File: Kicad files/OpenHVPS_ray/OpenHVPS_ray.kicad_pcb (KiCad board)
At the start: 2 copper layers, 40.6 x 20.8 mm, 67 parts, among them J2 Conn_01x03_Male, Q1 FQT7N10, Q2 BC846A, Q3 MMDT3906, U1 MAX6008AEUR+T, U2 74HC14, U3 MAX4162, U4 CD14538BM

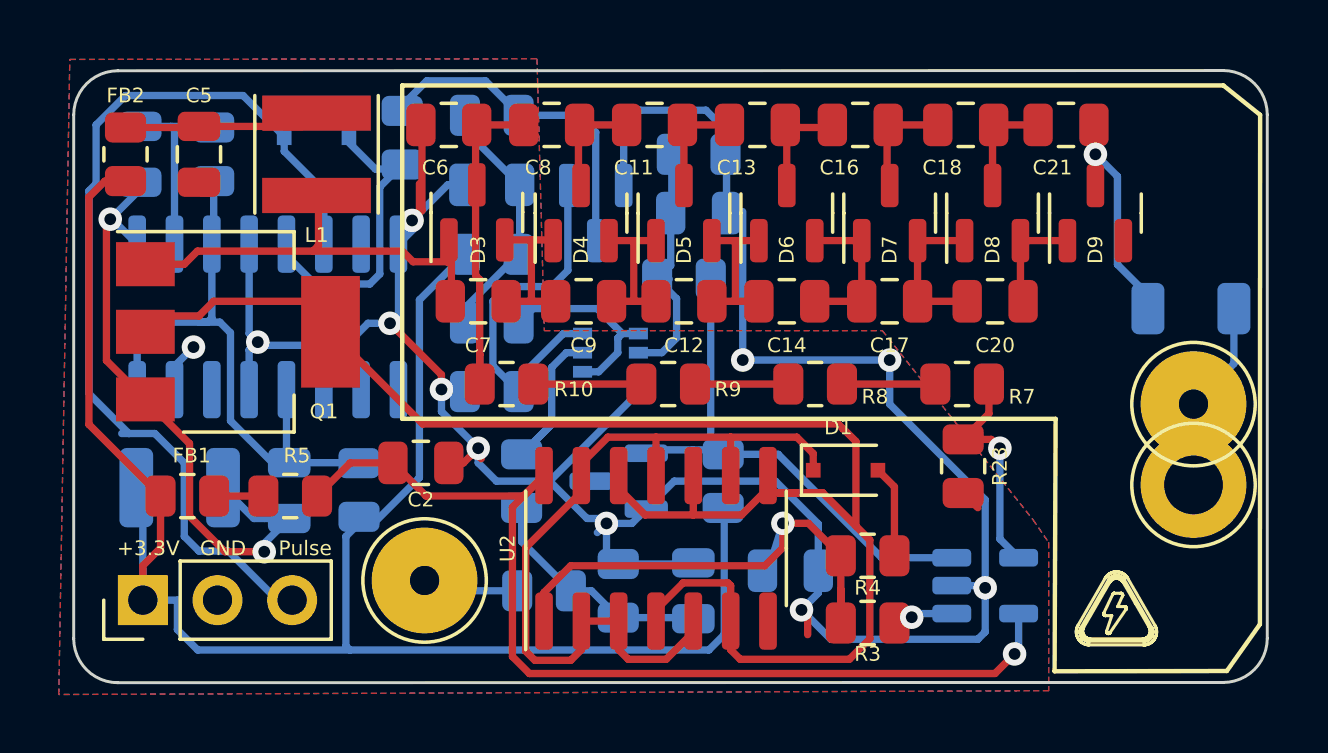
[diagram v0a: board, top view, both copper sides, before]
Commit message: Added a fuse for reverse polarity protection
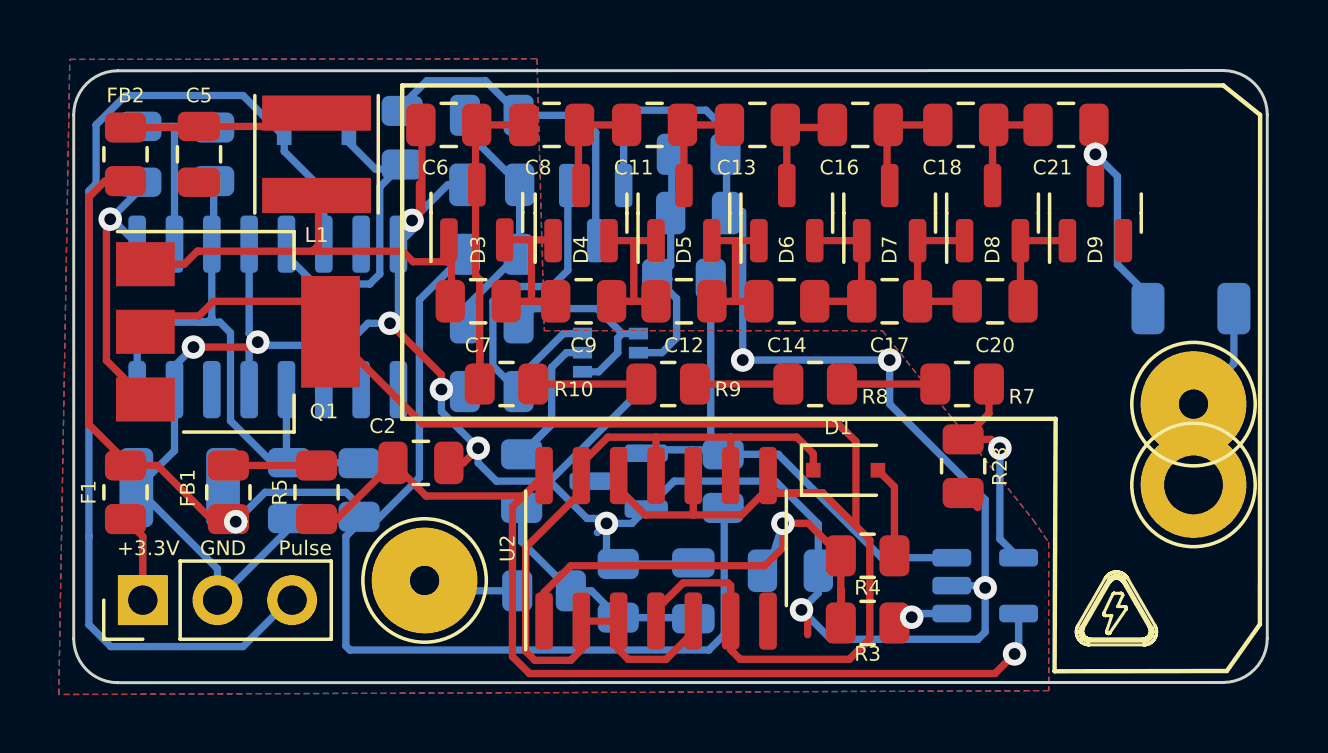
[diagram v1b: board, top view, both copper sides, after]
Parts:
- added F1: 1.62A, Resistor_SMD:R_0805_2012Metric, F.Cu at (128.0, 71.5)
- moved FB1 1.40 mm to (131.5, 71.5), turned to 90 degrees
- moved R5 0.91 mm to (134.5, 71.5), turned to 90 degrees
- turned C4 to 180 degrees
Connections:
- J2 pad 1: +3V3 -> Net-(J1-Pad1)
- Q1 pad 3: GND -> Net-(Q1-Pad3)
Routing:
- net +3V3: track 63.2 -> 56.2 mm, vias 0 -> 1
- net Net-(D2-Pad2): track 32.5 -> 38.0 mm
- net GND: track 121.0 -> 124.4 mm, vias 13 -> 12
- net Net-(J1-Pad1): track 0.00 -> 3.00 mm
- net Net-(FB1-Pad2): track 1.68 -> 3.00 mm
